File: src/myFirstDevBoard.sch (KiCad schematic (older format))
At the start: 36 parts, among them J1 Conn_01x15_Male, J2 Conn_01x15_Male, Q1 BC550, Q2 BC550, Q3 BC550, SW1 SW_Push, SW2 SW_Push, SW3 SW_Push, SW4 SW_Push, SW5 SW_SLIDER, SW6 SW_SLIDER

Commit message: making v0.2
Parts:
- A1: footprint Module:Arduino_Nano -> lib:Arduino_Nano_oval
- BZ1: footprint Buzzer_Beeper:Buzzer_12x9.5RM7.6 -> lib:Buzzer_12x9.5RM7.6_oval
- D1, D2, D3, D4, D5, D6, D7, D8, D9: footprint lib:LED_D5.0mm-4_RGB -> lib:LED_D5.0mm-4_RGB_wide
- R1, R10, R11, R12, R13, R2, R3, R4, R5, R6, R7, R8, R9: footprint Resistor_THT:R_Axial_DIN0207_L6.3mm_D2.5mm_P10.16mm_Horizontal -> lib:R_Axial_DIN0207_L6.3mm_D2.5mm_P10.16mm_Horizontal_oval
- RV1: footprint Potentiometer_THT:Potentiometer_Alps_RK163_Single_Horizontal -> lib:Potentiometer_Alps_RK163_Single_Horizontal_oval
- SW1, SW2, SW3, SW4: footprint Button_Switch_THT:SW_PUSH-12mm -> lib:SW_PUSH-12mm_with_poles
- SW5, SW6: footprint lib:PinHeader_1x03_P2.54mm_Vertical -> lib:PinHeader_1x03_P2.54mm_Vertical_oval
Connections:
- net GND: now also RV1.3
- net pot: now also RV1.2; no longer RV1.3
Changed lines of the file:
@@
 EESchema Schematic File Version 4
-LIBS:bordje-cache
+LIBS:myFirstDevBoard-cache
 EELAYER 26 0
 EELAYER END
@@
 encoding utf-8
 Sheet 1 1
-Title ""
+Title "Schematic for My First Dev Board"
 Date ""
 Rev ""
-Comp ""
-Comment1 ""
+Comp "University of Applied Sciences Utrecht"
+Comment1 "HBO - ICT Computer engineering"
 Comment2 ""
 Comment3 ""
@@
 F 0 "A1" H 8600 1100 50  0000 C CNN
 F 1 "Arduino_Nano_v3.x" H 8600 1000 50  0000 C CNN
-F 2 "Module:Arduino_Nano" H 9300 1200 50  0001 L CNN
+F 2 "lib:Arduino_Nano_oval" H 9300 1200 50  0001 L CNN
 F 3 "http://www.mouser.com/pdfdocs/Gravitech_Arduino_Nano3_0.pdf" H 9150 1150 50  0001 C CNN
 	1    9150 2150
@@
 F 0 "R1" H 1270 1196 50  0000 L CNN
 F 1 "1kΩ" H 1270 1105 50  0000 L CNN
-F 2 "Resistor_THT:R_Axial_DIN0207_L6.3mm_D2.5mm_P10.16mm_Horizontal" V 1130 1150 50  0001 C CNN
+F 2 "lib:R_Axial_DIN0207_L6.3mm_D2.5mm_P10.16mm_Horizontal_oval" V 1130 1150 50  0001 C CNN
 F 3 "~" H 1200 1150 50  0001 C CNN
 	1    1200 1150
@@
 F 0 "R3" H 2370 1196 50  0000 L CNN
 F 1 "1kΩ" H 2370 1105 50  0000 L CNN
-F 2 "Resistor_THT:R_Axial_DIN0207_L6.3mm_D2.5mm_P10.16mm_Horizontal" V 2230 1150 50  0001 C CNN
+F 2 "lib:R_Axial_DIN0207_L6.3mm_D2.5mm_P10.16mm_Horizontal_oval" V 2230 1150 50  0001 C CNN
 F 3 "~" H 2300 1150 50  0001 C CNN
 	1    2300 1150
@@
 F 0 "R5" H 3470 1196 50  0000 L CNN
 F 1 "1kΩ" H 3470 1105 50  0000 L CNN
-F 2 "Resistor_THT:R_Axial_DIN0207_L6.3mm_D2.5mm_P10.16mm_Horizontal" V 3330 1150 50  0001 C CNN
+F 2 "lib:R_Axial_DIN0207_L6.3mm_D2.5mm_P10.16mm_Horizontal_oval" V 3330 1150 50  0001 C CNN
 F 3 "~" H 3400 1150 50  0001 C CNN
 	1    3400 1150
@@
 F 0 "R7" H 4570 1196 50  0000 L CNN
 F 1 "1kΩ" H 4570 1105 50  0000 L CNN
-F 2 "Resistor_THT:R_Axial_DIN0207_L6.3mm_D2.5mm_P10.16mm_Horizontal" V 4430 1150 50  0001 C CNN
+F 2 "lib:R_Axial_DIN0207_L6.3mm_D2.5mm_P10.16mm_Horizontal_oval" V 4430 1150 50  0001 C CNN
 F 3 "~" H 4500 1150 50  0001 C CNN
 	1    4500 1150
@@
 F 0 "R8" H 4570 2596 50  0000 L CNN
 F 1 "1kΩ" H 4570 2505 50  0000 L CNN
-F 2 "Resistor_THT:R_Axial_DIN0207_L6.3mm_D2.5mm_P10.16mm_Horizontal" V 4430 2550 50  0001 C CNN
+F 2 "lib:R_Axial_DIN0207_L6.3mm_D2.5mm_P10.16mm_Horizontal_oval" V 4430 2550 50  0001 C CNN
 F 3 "~" H 4500 2550 50  0001 C CNN
 	1    4500 2550
@@
 F 0 "R6" H 3470 2596 50  0000 L CNN
 F 1 "1kΩ" H 3470 2505 50  0000 L CNN
-F 2 "Resistor_THT:R_Axial_DIN0207_L6.3mm_D2.5mm_P10.16mm_Horizontal" V 3330 2550 50  0001 C CNN
+F 2 "lib:R_Axial_DIN0207_L6.3mm_D2.5mm_P10.16mm_Horizontal_oval" V 3330 2550 50  0001 C CNN
 F 3 "~" H 3400 2550 50  0001 C CNN
 	1    3400 2550
@@
 F 0 "R4" H 2370 2596 50  0000 L CNN
 F 1 "1kΩ" H 2370 2505 50  0000 L CNN
-F 2 "Resistor_THT:R_Axial_DIN0207_L6.3mm_D2.5mm_P10.16mm_Horizontal" V 2230 2550 50  0001 C CNN
+F 2 "lib:R_Axial_DIN0207_L6.3mm_D2.5mm_P10.16mm_Horizontal_oval" V 2230 2550 50  0001 C CNN
 F 3 "~" H 2300 2550 50  0001 C CNN
 	1    2300 2550
@@
 F 0 "R2" H 1270 2596 50  0000 L CNN
 F 1 "1kΩ" H 1270 2505 50  0000 L CNN
-F 2 "Resistor_THT:R_Axial_DIN0207_L6.3mm_D2.5mm_P10.16mm_Horizontal" V 1130 2550 50  0001 C CNN
+F 2 "lib:R_Axial_DIN0207_L6.3mm_D2.5mm_P10.16mm_Horizontal_oval" V 1130 2550 50  0001 C CNN
 F 3 "~" H 1200 2550 50  0001 C CNN
 	1    1200 2550
@@
 F 0 "R10" H 7241 2204 50  0000 R CNN
 F 1 "1kΩ" H 7241 2295 50  0000 R CNN
-F 2 "Resistor_THT:R_Axial_DIN0207_L6.3mm_D2.5mm_P10.16mm_Horizontal" H 7300 2250 50  0001 C CNN
+F 2 "lib:R_Axial_DIN0207_L6.3mm_D2.5mm_P10.16mm_Horizontal_oval" H 7300 2250 50  0001 C CNN
 F 3 "~" H 7300 2250 50  0001 C CNN
 	1    7300 2250
@@
 F 0 "R9" V 6100 2200 50  0000 C CNN
 F 1 "1kΩ" V 6305 2250 50  0000 C CNN
-F 2 "Resistor_THT:R_Axial_DIN0207_L6.3mm_D2.5mm_P10.16mm_Horizontal" H 6200 2250 50  0001 C CNN
+F 2 "lib:R_Axial_DIN0207_L6.3mm_D2.5mm_P10.16mm_Horizontal_oval" H 6200 2250 50  0001 C CNN
 F 3 "~" H 6200 2250 50  0001 C CNN
 	1    6200 2250
@@
 F 0 "SW4" H 5800 5600 50  0000 C CNN
 F 1 "SW_Push" H 5800 5894 50  0000 C CNN
-F 2 "Button_Switch_THT:SW_PUSH-12mm" H 5800 5900 50  0001 C CNN
+F 2 "lib:SW_PUSH-12mm_with_poles" H 5800 5900 50  0001 C CNN
 F 3 "" H 5800 5900 50  0001 C CNN
 	1    5800 5700
@@
 F 0 "SW3" H 5800 5200 50  0000 C CNN
 F 1 "SW_Push" H 5800 5494 50  0000 C CNN
-F 2 "Button_Switch_THT:SW_PUSH-12mm" H 5800 5500 50  0001 C CNN
+F 2 "lib:SW_PUSH-12mm_with_poles" H 5800 5500 50  0001 C CNN
 F 3 "" H 5800 5500 50  0001 C CNN
 	1    5800 5300
@@
 F 0 "SW2" H 5800 4800 50  0000 C CNN
 F 1 "SW_Push" H 5800 5094 50  0000 C CNN
-F 2 "Button_Switch_THT:SW_PUSH-12mm" H 5800 5100 50  0001 C CNN
+F 2 "lib:SW_PUSH-12mm_with_poles" H 5800 5100 50  0001 C CNN
 F 3 "" H 5800 5100 50  0001 C CNN
 	1    5800 4900
@@
 F 0 "SW1" H 5800 4400 50  0000 C CNN
 F 1 "SW_Push" H 5800 4694 50  0000 C CNN
-F 2 "Button_Switch_THT:SW_PUSH-12mm" H 5800 4700 50  0001 C CNN
+F 2 "lib:SW_PUSH-12mm_with_poles" H 5800 4700 50  0001 C CNN
 F 3 "" H 5800 4700 50  0001 C CNN
 	1    5800 4500
@@
 F 0 "BZ1" H 2953 6029 50  0000 L CNN
 F 1 "Buzzer" H 2950 6450 50  0000 L CNN
-F 2 "Buzzer_Beeper:Buzzer_12x9.5RM7.6" V 2775 6100 50  0001 C CNN
+F 2 "lib:Buzzer_12x9.5RM7.6_oval" V 2775 6100 50  0001 C CNN
 F 3 "~" V 2775 6100 50  0001 C CNN
 	1    2800 6000
@@
 F 0 "R12" H 2670 5796 50  0000 L CNN
 F 1 "R" H 2670 5705 50  0000 L CNN
-F 2 "Resistor_THT:R_Axial_DIN0207_L6.3mm_D2.5mm_P10.16mm_Horizontal" V 2530 5750 50  0001 C CNN
+F 2 "lib:R_Axial_DIN0207_L6.3mm_D2.5mm_P10.16mm_Horizontal_oval" V 2530 5750 50  0001 C CNN
 F 3 "~" H 2600 5750 50  0001 C CNN
 	1    2600 5750
@@
 F 0 "SW5" H 4400 5035 50  0000 C CNN
 F 1 "SW_SLIDER" H 4400 4944 50  0000 C CNN
-F 2 "lib:PinHeader_1x03_P2.54mm_Vertical" H 4400 4750 50  0001 C CNN
+F 2 "lib:PinHeader_1x03_P2.54mm_Vertical_oval" H 4400 4750 50  0001 C CNN
 F 3 "" H 4400 4750 50  0001 C CNN
 	1    4400 4750
@@
 F 0 "SW6" H 4400 5585 50  0000 C CNN
 F 1 "SW_SLIDER" H 4400 5494 50  0000 C CNN
-F 2 "lib:PinHeader_1x03_P2.54mm_Vertical" H 4400 5300 50  0001 C CNN
+F 2 "lib:PinHeader_1x03_P2.54mm_Vertical_oval" H 4400 5300 50  0001 C CNN
 F 3 "" H 4400 5300 50  0001 C CNN
 	1    4400 5300
@@
 F 0 "R11" V 6650 2200 50  0000 C CNN
 F 1 "1kΩ" V 6855 2250 50  0000 C CNN
-F 2 "Resistor_THT:R_Axial_DIN0207_L6.3mm_D2.5mm_P10.16mm_Horizontal" H 6750 2250 50  0001 C CNN
+F 2 "lib:R_Axial_DIN0207_L6.3mm_D2.5mm_P10.16mm_Horizontal_oval" H 6750 2250 50  0001 C CNN
 F 3 "~" H 6750 2250 50  0001 C CNN
 	1    6750 2250
@@
 Wire Notes Line
 	10050 3550 8100 3550
-Text Label 7050 5250 2    50   ~ 0
+Text Label 7200 5000 0    50   ~ 0
 pot
 $Comp
@@
 F 0 "RV1" H 6980 5046 50  0000 R CNN
 F 1 "R_POT" H 6980 4955 50  0000 R CNN
-F 2 "Potentiometer_THT:Potentiometer_Alps_RK163_Single_Horizontal" H 7050 5000 50  0001 C CNN
+F 2 "lib:Potentiometer_Alps_RK163_Single_Horizontal_oval" H 7050 5000 50  0001 C CNN
 F 3 "~" H 7050 5000 50  0001 C CNN
 	1    7050 5000
@@
 Wire Notes Line
 	6700 5350 7450 5350
-Wire Wire Line
-	7050 5150 7050 5250
 $Comp
 L Connector:Conn_01x15_Male J2
@@
 F 0 "D1" V 1246 1170 50  0000 R CNN
 F 1 "LED_BGRA" V 1155 1170 50  0000 R CNN
-F 2 "lib:LED_D5.0mm-4_RGB" H 1200 1450 50  0001 C CNN
+F 2 "lib:LED_D5.0mm-4_RGB_wide" H 1200 1450 50  0001 C CNN
 F 3 "~" H 1200 1450 50  0001 C CNN
 	1    1200 1500
@@
 F 0 "D3" V 2346 1170 50  0000 R CNN
 F 1 "LED_BGRA" V 2255 1170 50  0000 R CNN
-F 2 "lib:LED_D5.0mm-4_RGB" H 2300 1450 50  0001 C CNN
+F 2 "lib:LED_D5.0mm-4_RGB_wide" H 2300 1450 50  0001 C CNN
 F 3 "~" H 2300 1450 50  0001 C CNN
 	1    2300 1500
@@
 F 0 "D5" V 3446 1170 50  0000 R CNN
 F 1 "LED_BGRA" V 3355 1170 50  0000 R CNN
-F 2 "lib:LED_D5.0mm-4_RGB" H 3400 1450 50  0001 C CNN
+F 2 "lib:LED_D5.0mm-4_RGB_wide" H 3400 1450 50  0001 C CNN
 F 3 "~" H 3400 1450 50  0001 C CNN
 	1    3400 1500
@@
 F 0 "D7" V 4546 1170 50  0000 R CNN
 F 1 "LED_BGRA" V 4455 1170 50  0000 R CNN
-F 2 "lib:LED_D5.0mm-4_RGB" H 4500 1450 50  0001 C CNN
+F 2 "lib:LED_D5.0mm-4_RGB_wide" H 4500 1450 50  0001 C CNN
 F 3 "~" H 4500 1450 50  0001 C CNN
 	1    4500 1500
@@
 F 0 "D2" V 1154 1870 50  0000 R CNN
 F 1 "LED_BGRA" V 1245 1870 50  0000 R CNN
-F 2 "lib:LED_D5.0mm-4_RGB" H 1200 2150 50  0001 C CNN
+F 2 "lib:LED_D5.0mm-4_RGB_wide" H 1200 2150 50  0001 C CNN
 F 3 "~" H 1200 2150 50  0001 C CNN
 	1    1200 2200
@@
 F 0 "D4" V 2254 1870 50  0000 R CNN
 F 1 "LED_BGRA" V 2345 1870 50  0000 R CNN
-F 2 "lib:LED_D5.0mm-4_RGB" H 2300 2150 50  0001 C CNN
+F 2 "lib:LED_D5.0mm-4_RGB_wide" H 2300 2150 50  0001 C CNN
 F 3 "~" H 2300 2150 50  0001 C CNN
 	1    2300 2200
@@
 F 0 "D6" V 3354 1870 50  0000 R CNN
 F 1 "LED_BGRA" V 3445 1870 50  0000 R CNN
-F 2 "lib:LED_D5.0mm-4_RGB" H 3400 2150 50  0001 C CNN
+F 2 "lib:LED_D5.0mm-4_RGB_wide" H 3400 2150 50  0001 C CNN
 F 3 "~" H 3400 2150 50  0001 C CNN
 	1    3400 2200
@@
 F 0 "D8" V 4454 1870 50  0000 R CNN
 F 1 "LED_BGRA" V 4545 1870 50  0000 R CNN
-F 2 "lib:LED_D5.0mm-4_RGB" H 4500 2150 50  0001 C CNN
+F 2 "lib:LED_D5.0mm-4_RGB_wide" H 4500 2150 50  0001 C CNN
 F 3 "~" H 4500 2150 50  0001 C CNN
 	1    4500 2200
@@
 F 0 "D9" V 5646 1170 50  0000 R CNN
 F 1 "LED_BGRA" V 5555 1170 50  0000 R CNN
-F 2 "lib:LED_D5.0mm-4_RGB" H 5600 1450 50  0001 C CNN
+F 2 "lib:LED_D5.0mm-4_RGB_wide" H 5600 1450 50  0001 C CNN
 F 3 "~" H 5600 1450 50  0001 C CNN
 	1    5600 1500
@@
 F 0 "R13" H 5670 1196 50  0000 L CNN
 F 1 "1kΩ" H 5670 1105 50  0000 L CNN
-F 2 "Resistor_THT:R_Axial_DIN0207_L6.3mm_D2.5mm_P10.16mm_Horizontal" V 5530 1150 50  0001 C CNN
+F 2 "lib:R_Axial_DIN0207_L6.3mm_D2.5mm_P10.16mm_Horizontal_oval" V 5530 1150 50  0001 C CNN
 F 3 "~" H 5600 1150 50  0001 C CNN
 	1    5600 1150
@@
 Wire Notes Line
 	750  2950 7600 2950
+$Comp
+L power:GND #PWR0106
+U 1 1 5C7E9B2A
+P 7050 5150
+F 0 "#PWR0106" H 7050 4900 50  0001 C CNN
+F 1 "GND" H 7055 4977 50  0000 C CNN
+F 2 "" H 7050 5150 50  0001 C CNN
+F 3 "" H 7050 5150 50  0001 C CNN
+	1    7050 5150
+	1    0    0    -1
+$EndComp
 $EndSCHEMATC

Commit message: adding v0.03
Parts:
- Q1, Q2, Q3: footprint Package_TO_SOT_THT:TO-92_Inline -> lib:TO-92_Inline_Wide_oval
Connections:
- net led9: now also A1.24 (A5), J2.9 (Pin_9); no longer A1.26 (A7), J2.11 (Pin_11)
- net sw5: now also A1.26 (A7), J2.11 (Pin_11); no longer A1.24 (A5), J2.9 (Pin_9)
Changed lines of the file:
@@
 F 0 "Q1" H 5750 2400 50  0000 L CNN
 F 1 "BC550" H 5700 2300 50  0000 L CNN
-F 2 "Package_TO_SOT_THT:TO-92_Inline" H 6200 2075 50  0001 L CIN
+F 2 "lib:TO-92_Inline_Wide_oval" H 6200 2075 50  0001 L CIN
 F 3 "http://www.fairchildsemi.com/ds/BC/BC547.pdf" H 6000 2150 50  0001 L CNN
 	1    6000 2150
@@
 F 0 "Q2" H 6400 2300 50  0000 L CNN
 F 1 "BC550" H 6350 2400 50  0000 L CNN
-F 2 "Package_TO_SOT_THT:TO-92_Inline" H 6750 2075 50  0001 L CIN
+F 2 "lib:TO-92_Inline_Wide_oval" H 6750 2075 50  0001 L CIN
 F 3 "http://www.fairchildsemi.com/ds/BC/BC547.pdf" H 6550 2150 50  0001 L CNN
 	1    6550 2150
@@
 F 0 "Q3" H 6900 2400 50  0000 L CNN
 F 1 "BC550" H 6800 2300 50  0000 L CNN
-F 2 "Package_TO_SOT_THT:TO-92_Inline" H 7300 2075 50  0001 L CIN
+F 2 "lib:TO-92_Inline_Wide_oval" H 7300 2075 50  0001 L CIN
 F 3 "http://www.fairchildsemi.com/ds/BC/BC547.pdf" H 7100 2150 50  0001 L CNN
 	1    7100 2150
@@
 Text Label 4200 5300 2    50   ~ 0
 sw6
-Text Label 9650 2650 0    50   ~ 0
+Text Label 9650 2850 0    50   ~ 0
 sw5
 Text Label 9650 2750 0    50   ~ 0
@@
 Text Label 9150 5050 0    50   ~ 0
 sw4
-Text Label 9150 4950 0    50   ~ 0
+Text Label 9150 4750 0    50   ~ 0
 sw5
 Text Label 9150 4850 0    50   ~ 0
 sw6
-Text Label 9150 4750 0    50   ~ 0
+Text Label 9150 4950 0    50   ~ 0
 led9
 $Comp
@@
 Text Notes 6800 1000 0    50   ~ 0
 Leds
-Text Label 9650 2850 0    50   ~ 0
+Text Label 9650 2650 0    50   ~ 0
 led9
 $Comp

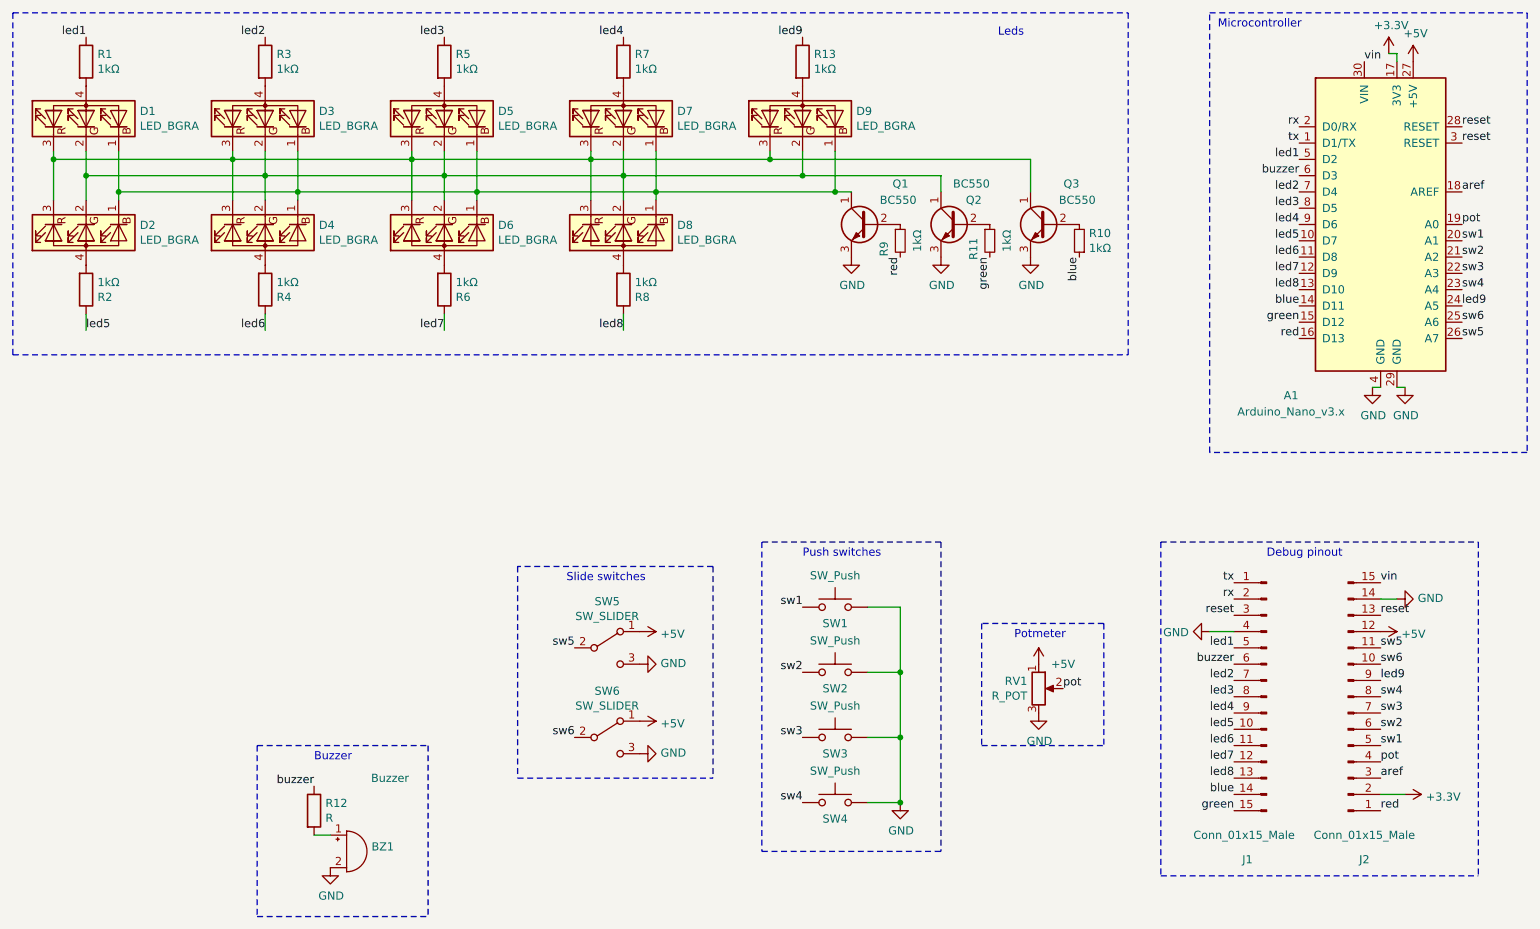
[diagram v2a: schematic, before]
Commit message: changing silkscreen to be organised
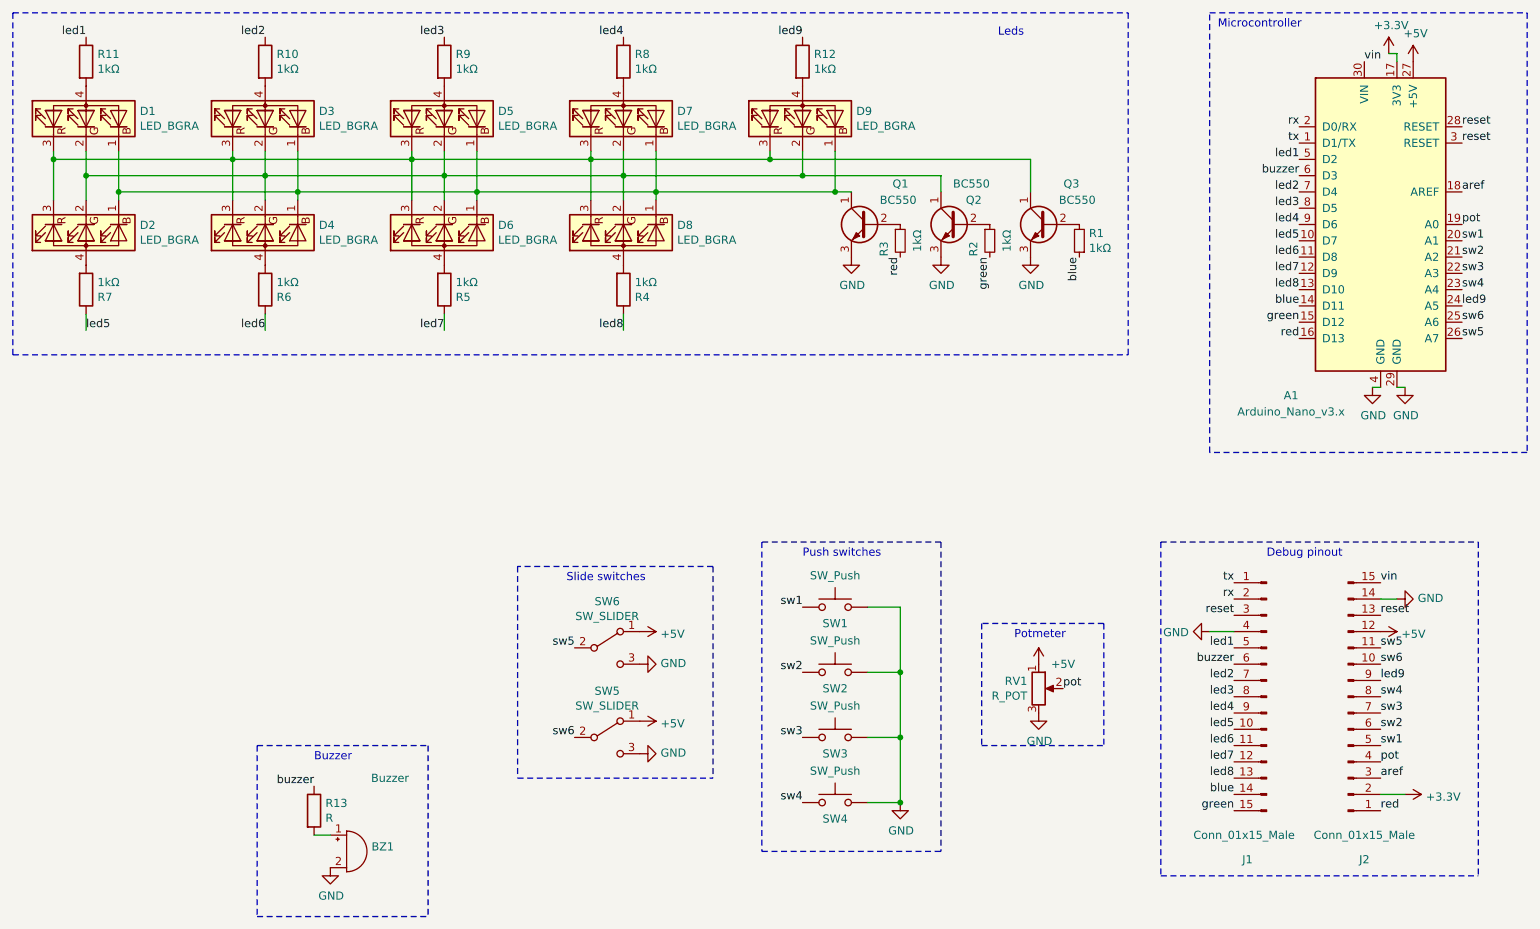
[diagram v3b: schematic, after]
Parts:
- renumbered R10 to R1, R3 to R10, R1 to R11, R13 to R12, R12 to R13, R11 to R2, R9 to R3, R8 to R4, R6 to R5, R4 to R6, R2 to R7, R7 to R8, R5 to R9, SW6 to SW5, SW5 to SW6
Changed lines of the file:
@@
 $EndComp
 $Comp
-L Device:R R1
+L Device:R R11
 U 1 1 5C6AD5EF
 P 1200 1150
-F 0 "R1" H 1270 1196 50  0000 L CNN
+F 0 "R11" H 1270 1196 50  0000 L CNN
 F 1 "1kΩ" H 1270 1105 50  0000 L CNN
 F 2 "lib:R_Axial_DIN0207_L6.3mm_D2.5mm_P10.16mm_Horizontal_oval" V 1130 1150 50  0001 C CNN
@@
 $EndComp
 $Comp
-L Device:R R3
+L Device:R R10
 U 1 1 5C6AD6E4
 P 2300 1150
-F 0 "R3" H 2370 1196 50  0000 L CNN
+F 0 "R10" H 2370 1196 50  0000 L CNN
 F 1 "1kΩ" H 2370 1105 50  0000 L CNN
 F 2 "lib:R_Axial_DIN0207_L6.3mm_D2.5mm_P10.16mm_Horizontal_oval" V 2230 1150 50  0001 C CNN
@@
 $EndComp
 $Comp
-L Device:R R5
+L Device:R R9
 U 1 1 5C6AD744
 P 3400 1150
-F 0 "R5" H 3470 1196 50  0000 L CNN
+F 0 "R9" H 3470 1196 50  0000 L CNN
 F 1 "1kΩ" H 3470 1105 50  0000 L CNN
 F 2 "lib:R_Axial_DIN0207_L6.3mm_D2.5mm_P10.16mm_Horizontal_oval" V 3330 1150 50  0001 C CNN
@@
 $EndComp
 $Comp
-L Device:R R7
+L Device:R R8
 U 1 1 5C6AD780
 P 4500 1150
-F 0 "R7" H 4570 1196 50  0000 L CNN
+F 0 "R8" H 4570 1196 50  0000 L CNN
 F 1 "1kΩ" H 4570 1105 50  0000 L CNN
 F 2 "lib:R_Axial_DIN0207_L6.3mm_D2.5mm_P10.16mm_Horizontal_oval" V 4430 1150 50  0001 C CNN
@@
 $EndComp
 $Comp
-L Device:R R8
+L Device:R R4
 U 1 1 5C6AD7CE
 P 4500 2550
-F 0 "R8" H 4570 2596 50  0000 L CNN
+F 0 "R4" H 4570 2596 50  0000 L CNN
 F 1 "1kΩ" H 4570 2505 50  0000 L CNN
 F 2 "lib:R_Axial_DIN0207_L6.3mm_D2.5mm_P10.16mm_Horizontal_oval" V 4430 2550 50  0001 C CNN
@@
 $EndComp
 $Comp
-L Device:R R6
+L Device:R R5
 U 1 1 5C6AD83C
 P 3400 2550
-F 0 "R6" H 3470 2596 50  0000 L CNN
+F 0 "R5" H 3470 2596 50  0000 L CNN
 F 1 "1kΩ" H 3470 2505 50  0000 L CNN
 F 2 "lib:R_Axial_DIN0207_L6.3mm_D2.5mm_P10.16mm_Horizontal_oval" V 3330 2550 50  0001 C CNN
@@
 $EndComp
 $Comp
-L Device:R R4
+L Device:R R6
 U 1 1 5C6AD886
 P 2300 2550
-F 0 "R4" H 2370 2596 50  0000 L CNN
+F 0 "R6" H 2370 2596 50  0000 L CNN
 F 1 "1kΩ" H 2370 2505 50  0000 L CNN
 F 2 "lib:R_Axial_DIN0207_L6.3mm_D2.5mm_P10.16mm_Horizontal_oval" V 2230 2550 50  0001 C CNN
@@
 $EndComp
 $Comp
-L Device:R R2
+L Device:R R7
 U 1 1 5C6AD8DA
 P 1200 2550
-F 0 "R2" H 1270 2596 50  0000 L CNN
+F 0 "R7" H 1270 2596 50  0000 L CNN
 F 1 "1kΩ" H 1270 2505 50  0000 L CNN
 F 2 "lib:R_Axial_DIN0207_L6.3mm_D2.5mm_P10.16mm_Horizontal_oval" V 1130 2550 50  0001 C CNN
@@
 	4300 1750 3200 1750
 $Comp
-L Device:R_Small R10
+L Device:R_Small R1
 U 1 1 5C6C9A5E
 P 7300 2250
-F 0 "R10" H 7241 2204 50  0000 R CNN
+F 0 "R1" H 7241 2204 50  0000 R CNN
 F 1 "1kΩ" H 7241 2295 50  0000 R CNN
 F 2 "lib:R_Axial_DIN0207_L6.3mm_D2.5mm_P10.16mm_Horizontal_oval" H 7300 2250 50  0001 C CNN
@@
 $EndComp
 $Comp
-L Device:R_Small R9
+L Device:R_Small R3
 U 1 1 5C6CE760
 P 6200 2250
-F 0 "R9" V 6100 2200 50  0000 C CNN
+F 0 "R3" V 6100 2200 50  0000 C CNN
 F 1 "1kΩ" V 6305 2250 50  0000 C CNN
 F 2 "lib:R_Axial_DIN0207_L6.3mm_D2.5mm_P10.16mm_Horizontal_oval" H 6200 2250 50  0001 C CNN
@@
 $EndComp
 $Comp
-L Device:R R12
+L Device:R R13
 U 1 1 5C6E5EC9
 P 2600 5750
-F 0 "R12" H 2670 5796 50  0000 L CNN
+F 0 "R13" H 2670 5796 50  0000 L CNN
 F 1 "R" H 2670 5705 50  0000 L CNN
 F 2 "lib:R_Axial_DIN0207_L6.3mm_D2.5mm_P10.16mm_Horizontal_oval" V 2530 5750 50  0001 C CNN
@@
 	9250 3150 9300 3150
 $Comp
-L Switch:SW_SPDT SW5
+L Switch:SW_SPDT SW6
 U 1 1 5C6F28A7
 P 4400 4750
-F 0 "SW5" H 4400 5035 50  0000 C CNN
+F 0 "SW6" H 4400 5035 50  0000 C CNN
 F 1 "SW_SLIDER" H 4400 4944 50  0000 C CNN
 F 2 "lib:PinHeader_1x03_P2.54mm_Vertical_oval" H 4400 4750 50  0001 C CNN
@@
 $EndComp
 $Comp
-L Switch:SW_SPDT SW6
+L Switch:SW_SPDT SW5
 U 1 1 5C6F2DDC
 P 4400 5300
-F 0 "SW6" H 4400 5585 50  0000 C CNN
+F 0 "SW5" H 4400 5585 50  0000 C CNN
 F 1 "SW_SLIDER" H 4400 5494 50  0000 C CNN
 F 2 "lib:PinHeader_1x03_P2.54mm_Vertical_oval" H 4400 5300 50  0001 C CNN
@@
 	6450 1850 6450 1950
 $Comp
-L Device:R_Small R11
+L Device:R_Small R2
 U 1 1 5C71947B
 P 6750 2250
-F 0 "R11" V 6650 2200 50  0000 C CNN
+F 0 "R2" V 6650 2200 50  0000 C CNN
 F 1 "1kΩ" V 6855 2250 50  0000 C CNN
 F 2 "lib:R_Axial_DIN0207_L6.3mm_D2.5mm_P10.16mm_Horizontal_oval" H 6750 2250 50  0001 C CNN
@@
 $EndComp
 $Comp
-L Device:R R13
+L Device:R R12
 U 1 1 5C7471D9
 P 5600 1150
-F 0 "R13" H 5670 1196 50  0000 L CNN
+F 0 "R12" H 5670 1196 50  0000 L CNN
 F 1 "1kΩ" H 5670 1105 50  0000 L CNN
 F 2 "lib:R_Axial_DIN0207_L6.3mm_D2.5mm_P10.16mm_Horizontal_oval" V 5530 1150 50  0001 C CNN
